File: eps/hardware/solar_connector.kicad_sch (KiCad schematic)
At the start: 2 parts

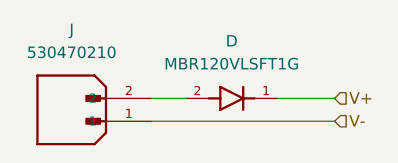
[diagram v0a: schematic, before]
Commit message: begin implementing battery charger
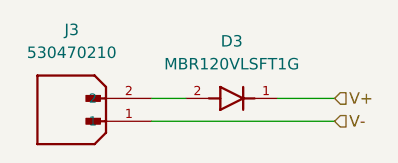
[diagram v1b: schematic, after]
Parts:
- renumbered D to D3, J to J3
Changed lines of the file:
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@@
 		(dnp no)
 		(fields_autoplaced yes)
-		(property "Reference" "D"
+		(property "Reference" "D?"
 			(at 148.59 95.25 0)
 			(effects
@@
 				(path "/c3008a62-3f93-44d6-ac6c-3e783bffd7ae/30b9d4bf-41af-4179-8f39-6660591a15e9"
 					(reference "D2")
+					(unit 1)
+				)
+				(path "/c3008a62-3f93-44d6-ac6c-3e783bffd7ae/3a5e5b2a-9588-4401-bdab-8a874c133434"
+					(reference "D?")
 					(unit 1)
 				)
@@
 		(dnp no)
 		(fields_autoplaced yes)
-		(property "Reference" "J"
+		(property "Reference" "J?"
 			(at 130.81 93.98 0)
 			(effects
@@
 					(unit 1)
 				)
+				(path "/c3008a62-3f93-44d6-ac6c-3e783bffd7ae/3a5e5b2a-9588-4401-bdab-8a874c133434"
+					(reference "J?")
+					(unit 1)
+				)
